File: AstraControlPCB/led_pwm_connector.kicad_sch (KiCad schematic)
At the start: 12 parts, among them CN5 JST_VH_8PIN_10A_250V

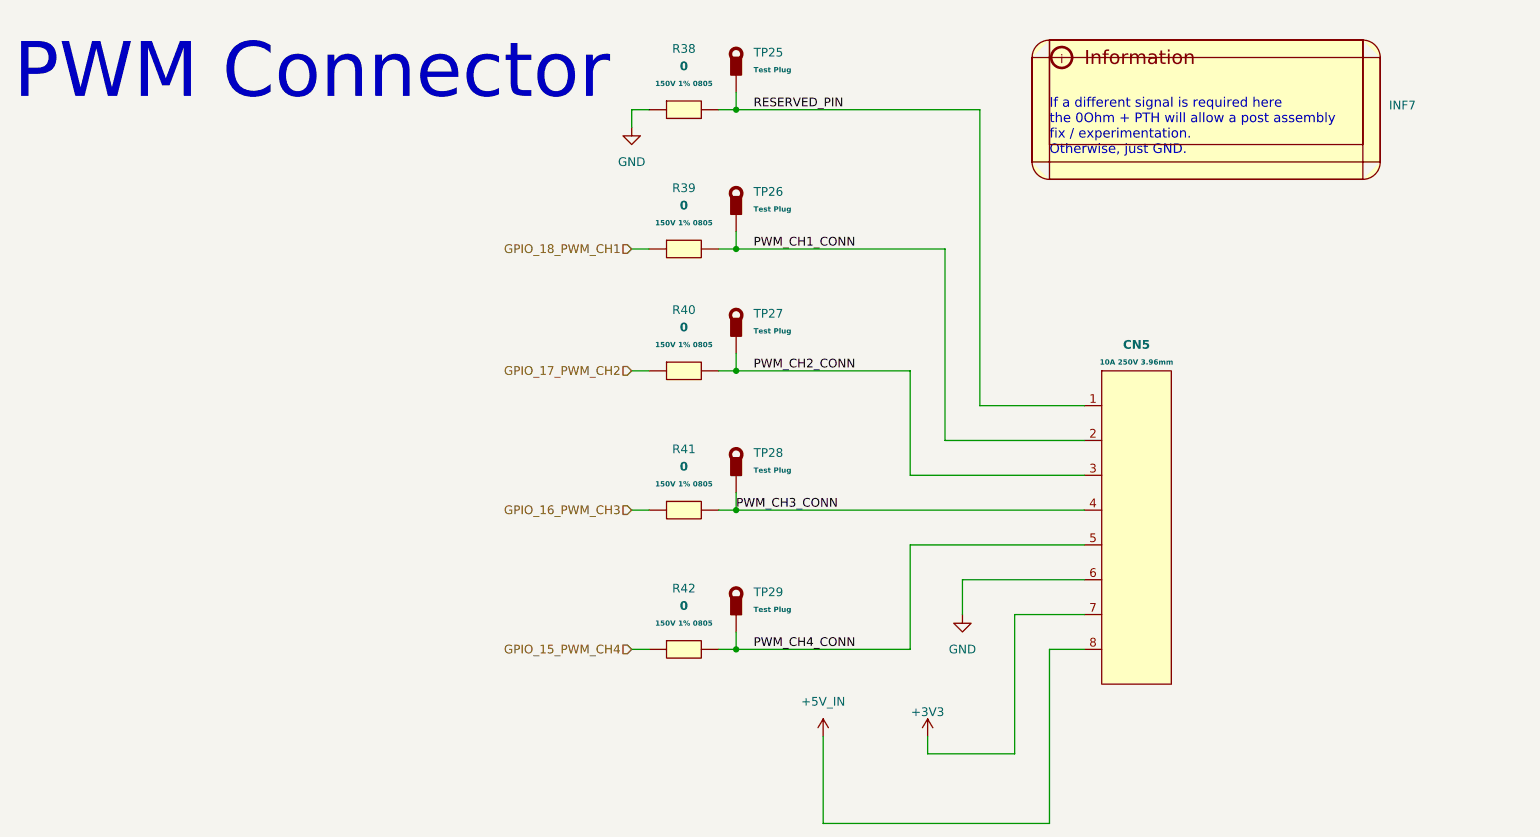
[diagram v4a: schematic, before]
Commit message: New inductor that is in stock, updated rs485 ic layout to put caps closer
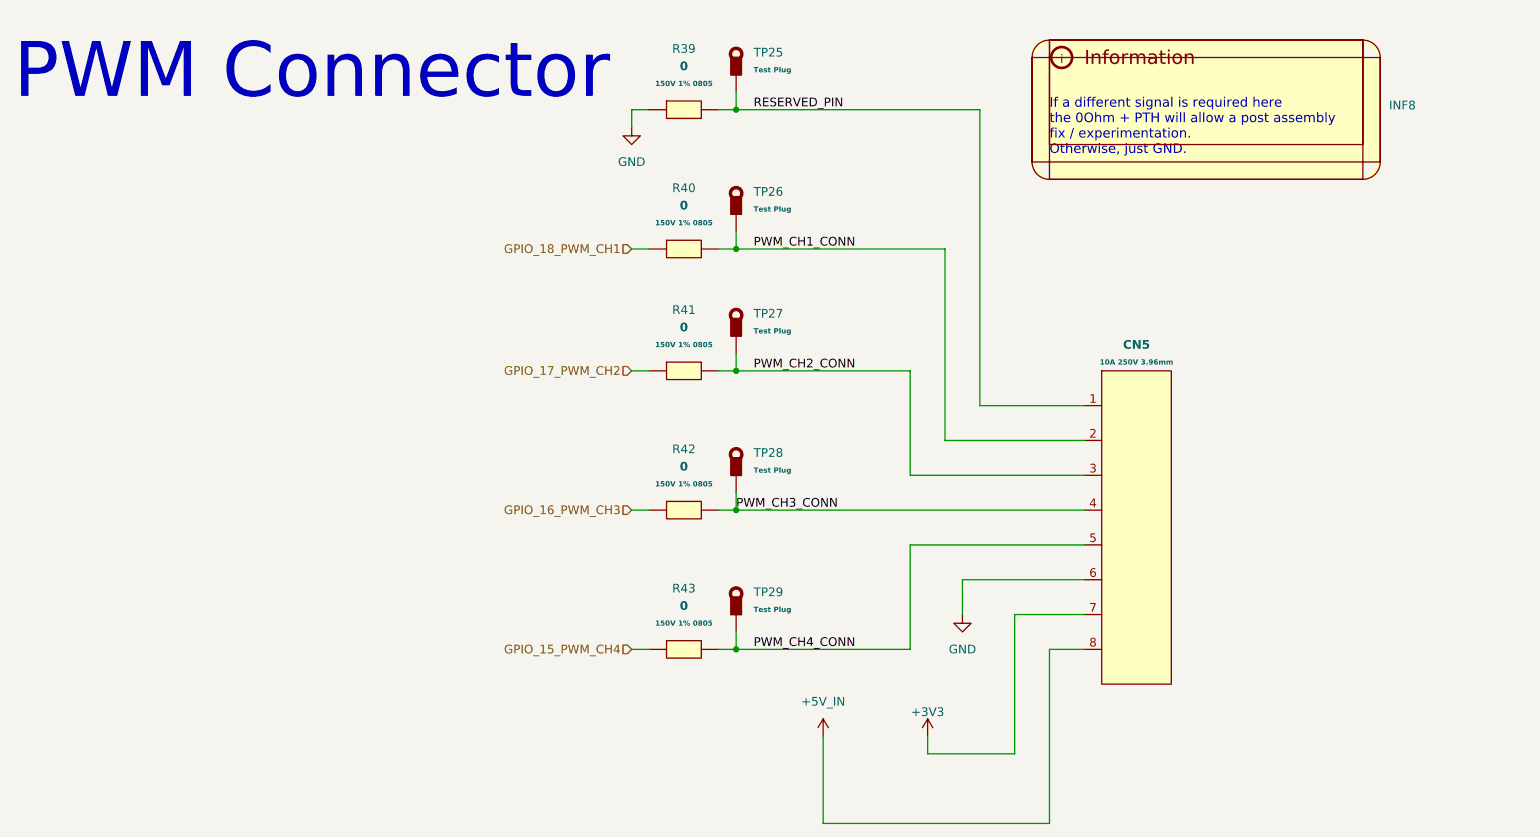
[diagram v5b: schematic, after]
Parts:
- renumbered INF7 to INF8, R38 to R39, R39 to R40, R40 to R41, R41 to R42, R42 to R43
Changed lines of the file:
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@@
 		(dnp no)
 		(fields_autoplaced yes)
-		(property "Reference" "#PWR072"
+		(property "Reference" "#PWR073"
 			(at 137.16 130.81 0)
 			(effects
@@
 			(project "AstraControl"
 				(path "/9a751838-dce8-4d69-8a02-736625ac74e7/0db21d8e-3390-4d67-877f-0e5d98e37848/e7f4ae23-1ac9-4fa3-959c-a78f85f3f546"
-					(reference "#PWR072")
+					(reference "#PWR073")
 					(unit 1)
 				)
@@
 		(on_board yes)
 		(dnp no)
-		(property "Reference" "#PWR073"
+		(property "Reference" "#PWR074"
 			(at 152.4 130.81 0)
 			(effects
@@
 			(project "AstraControl"
 				(path "/9a751838-dce8-4d69-8a02-736625ac74e7/0db21d8e-3390-4d67-877f-0e5d98e37848/e7f4ae23-1ac9-4fa3-959c-a78f85f3f546"
-					(reference "#PWR073")
+					(reference "#PWR074")
 					(unit 1)
 				)
@@
 		(dnp no)
 		(fields_autoplaced yes)
-		(property "Reference" "R38"
+		(property "Reference" "R39"
 			(at 116.84 26.67 0)
 			(effects
@@
 			(project "AstraControl"
 				(path "/9a751838-dce8-4d69-8a02-736625ac74e7/0db21d8e-3390-4d67-877f-0e5d98e37848/e7f4ae23-1ac9-4fa3-959c-a78f85f3f546"
-					(reference "R38")
+					(reference "R39")
 					(unit 1)
 				)
@@
 		(dnp no)
 		(fields_autoplaced yes)
-		(property "Reference" "#PWR074"
+		(property "Reference" "#PWR075"
 			(at 157.48 115.57 0)
 			(effects
@@
 			(project "AstraControl"
 				(path "/9a751838-dce8-4d69-8a02-736625ac74e7/0db21d8e-3390-4d67-877f-0e5d98e37848/e7f4ae23-1ac9-4fa3-959c-a78f85f3f546"
-					(reference "#PWR074")
+					(reference "#PWR075")
 					(unit 1)
 				)
@@
 		(dnp no)
 		(fields_autoplaced yes)
-		(property "Reference" "R40"
+		(property "Reference" "R41"
 			(at 116.84 64.77 0)
 			(effects
@@
 			(project "AstraControl"
 				(path "/9a751838-dce8-4d69-8a02-736625ac74e7/0db21d8e-3390-4d67-877f-0e5d98e37848/e7f4ae23-1ac9-4fa3-959c-a78f85f3f546"
-					(reference "R40")
+					(reference "R41")
 					(unit 1)
 				)
@@
 		(dnp no)
 		(fields_autoplaced yes)
-		(property "Reference" "R39"
+		(property "Reference" "R40"
 			(at 116.84 46.99 0)
 			(effects
@@
 			(project "AstraControl"
 				(path "/9a751838-dce8-4d69-8a02-736625ac74e7/0db21d8e-3390-4d67-877f-0e5d98e37848/e7f4ae23-1ac9-4fa3-959c-a78f85f3f546"
-					(reference "R39")
+					(reference "R40")
 					(unit 1)
 				)
@@
 		(dnp no)
 		(fields_autoplaced yes)
-		(property "Reference" "INF7"
+		(property "Reference" "INF8"
 			(at 219.71 34.9249 0)
 			(effects
@@
 			(project ""
 				(path "/9a751838-dce8-4d69-8a02-736625ac74e7/0db21d8e-3390-4d67-877f-0e5d98e37848/e7f4ae23-1ac9-4fa3-959c-a78f85f3f546"
-					(reference "INF7")
+					(reference "INF8")
 					(unit 1)
 				)
@@
 		(dnp no)
 		(fields_autoplaced yes)
-		(property "Reference" "#PWR071"
+		(property "Reference" "#PWR072"
 			(at 109.22 44.45 0)
 			(effects
@@
 			(project "AstraControl"
 				(path "/9a751838-dce8-4d69-8a02-736625ac74e7/0db21d8e-3390-4d67-877f-0e5d98e37848/e7f4ae23-1ac9-4fa3-959c-a78f85f3f546"
-					(reference "#PWR071")
+					(reference "#PWR072")
 					(unit 1)
 				)
@@
 		(dnp no)
 		(fields_autoplaced yes)
-		(property "Reference" "R42"
+		(property "Reference" "R43"
 			(at 116.84 105.41 0)
 			(effects
@@
 			(project "AstraControl"
 				(path "/9a751838-dce8-4d69-8a02-736625ac74e7/0db21d8e-3390-4d67-877f-0e5d98e37848/e7f4ae23-1ac9-4fa3-959c-a78f85f3f546"
-					(reference "R42")
+					(reference "R43")
 					(unit 1)
 				)
@@
 		(dnp no)
 		(fields_autoplaced yes)
-		(property "Reference" "R41"
+		(property "Reference" "R42"
 			(at 116.84 85.09 0)
 			(effects
@@
 			(project "AstraControl"
 				(path "/9a751838-dce8-4d69-8a02-736625ac74e7/0db21d8e-3390-4d67-877f-0e5d98e37848/e7f4ae23-1ac9-4fa3-959c-a78f85f3f546"
-					(reference "R41")
-					(unit 1)
-				)
+					(reference "R42")
+					(unit 1)
+				)

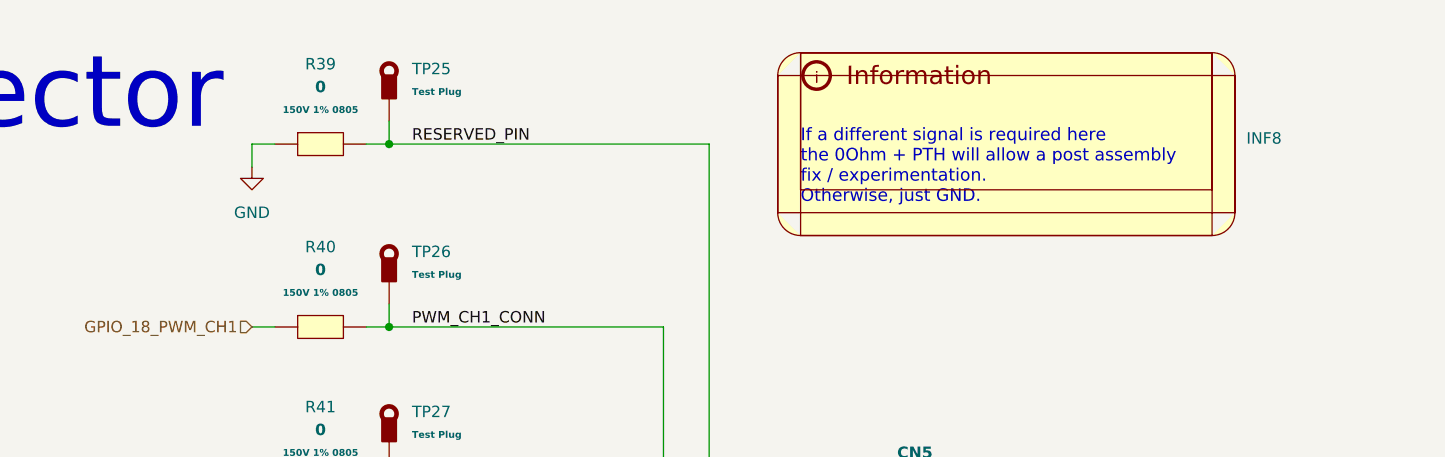
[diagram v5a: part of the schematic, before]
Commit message: Fix silkscreen on copper, add GPIO 8 to connector
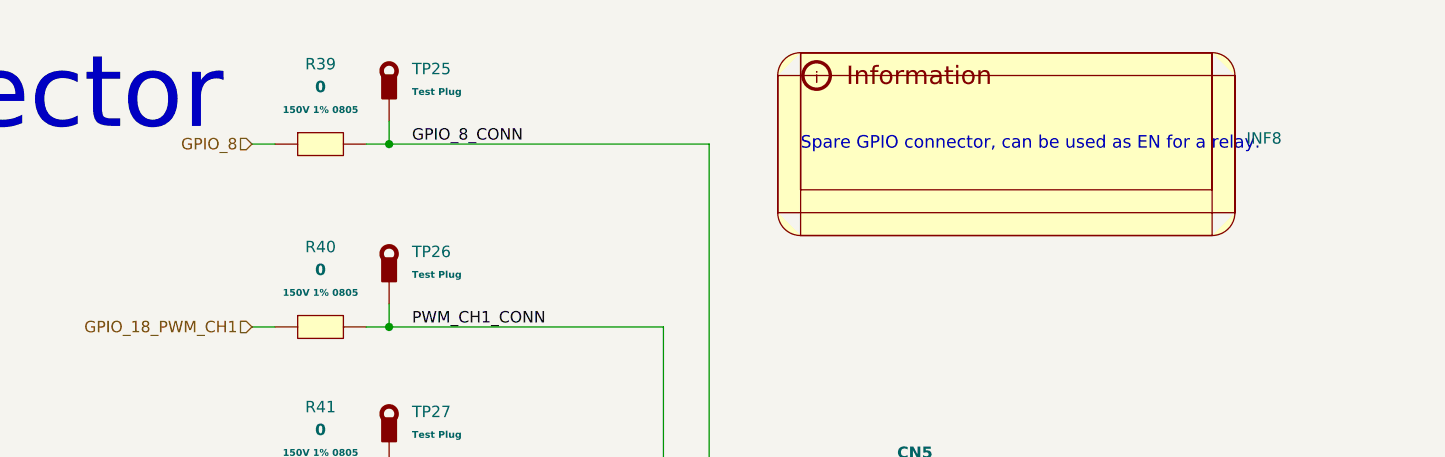
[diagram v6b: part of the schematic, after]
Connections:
- net GND: no longer R39.1
- net RESERVED_PIN renamed GPIO_8_CONN
- new net GPIO_8: R39.1
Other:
- note added: "Spare GPIO connector, can be used as EN for a relay."
- note removed: "If a different signal is required here the 0Ohm + PTH will allow a post assembly fix / experimentation. Otherwise, just GND."
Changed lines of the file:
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@@
-	(wire
-		(pts
-			(xy 109.22 35.56) (xy 109.22 38.1)
-		)
-		(stroke
-			(width 0)
-			(type default)
-		)
-	)
 	(wire
 		(pts
@@
 		)
 	)
-	(text "If a different signal is required here \nthe 0Ohm + PTH will allow a post assembly\nfix / experimentation.\nOtherwise, just GND."
+	(text "Spare GPIO connector, can be used as EN for a relay."
 		(exclude_from_sim no)
-		(at 170.18 38.1 0)
+		(at 170.18 35.56 0)
 		(effects
 			(font
@@
 		)
 	)
-	(label "RESERVED_PIN"
+	(label "GPIO_8_CONN"
 		(at 127 35.56 0)
 		(fields_autoplaced yes)
@@
 		(shape input)
 		(at 109.22 73.66 180)
+		(fields_autoplaced yes)
+		(effects
+			(font
+				(size 1.27 1.27)
+			)
+			(justify right)
+		)
+	)
+	(hierarchical_label "GPIO_8"
+		(shape input)
+		(at 109.22 35.56 180)
 		(fields_autoplaced yes)
 		(effects
@@
 		(dnp no)
 		(fields_autoplaced yes)
-		(property "Reference" "#PWR073"
+		(property "Reference" "#PWR072"
 			(at 137.16 130.81 0)
 			(effects
@@
 			(project "AstraControl"
 				(path "/9a751838-dce8-4d69-8a02-736625ac74e7/0db21d8e-3390-4d67-877f-0e5d98e37848/e7f4ae23-1ac9-4fa3-959c-a78f85f3f546"
-					(reference "#PWR073")
+					(reference "#PWR072")
 					(unit 1)
 				)
@@
 		(on_board yes)
 		(dnp no)
-		(property "Reference" "#PWR074"
+		(property "Reference" "#PWR073"
 			(at 152.4 130.81 0)
 			(effects
@@
 			(project "AstraControl"
 				(path "/9a751838-dce8-4d69-8a02-736625ac74e7/0db21d8e-3390-4d67-877f-0e5d98e37848/e7f4ae23-1ac9-4fa3-959c-a78f85f3f546"
-					(reference "#PWR074")
+					(reference "#PWR073")
 					(unit 1)
 				)
@@
 		(dnp no)
 		(fields_autoplaced yes)
-		(property "Reference" "#PWR075"
+		(property "Reference" "#PWR074"
 			(at 157.48 115.57 0)
 			(effects
@@
 			(project "AstraControl"
 				(path "/9a751838-dce8-4d69-8a02-736625ac74e7/0db21d8e-3390-4d67-877f-0e5d98e37848/e7f4ae23-1ac9-4fa3-959c-a78f85f3f546"
-					(reference "#PWR075")
+					(reference "#PWR074")
 					(unit 1)
 				)
@@
 					(unit 1)
 				)
-			)
-		)
-	)
-	(symbol
-		(lib_id "power:GND")
-		(at 109.22 38.1 0)
-		(unit 1)
-		(exclude_from_sim no)
-		(in_bom yes)
-		(on_board yes)
-		(dnp no)
-		(fields_autoplaced yes)
-		(property "Reference" "#PWR072"
-			(at 109.22 44.45 0)
-			(effects
-				(font
-					(size 1.27 1.27)
-				)
-				(hide yes)
-			)
-		)
-		(property "Value" "GND"
-			(at 109.22 43.18 0)
-			(effects
-				(font
-					(size 1.27 1.27)
-				)
-			)
-		)
-		(property "Footprint" ""
-			(at 109.22 38.1 0)
-			(effects
-				(font
-					(size 1.27 1.27)
-				)
-				(hide yes)
-			)
-		)
-		(property "Datasheet" ""
-			(at 109.22 38.1 0)
-			(effects
-				(font
-					(size 1.27 1.27)
-				)
-				(hide yes)
-			)
-		)
-		(property "Description" "Power symbol creates a global label with name \"GND\" , ground"
-			(at 109.22 38.1 0)
-			(effects
-				(font
-					(size 1.27 1.27)
-				)
-				(hide yes)
-			)
-		)
-		(pin "1"
-		)
-		(instances
-			(project "AstraControl"
-				(path "/9a751838-dce8-4d69-8a02-736625ac74e7/0db21d8e-3390-4d67-877f-0e5d98e37848/e7f4ae23-1ac9-4fa3-959c-a78f85f3f546"
-					(reference "#PWR072")
-					(unit 1)
-				)

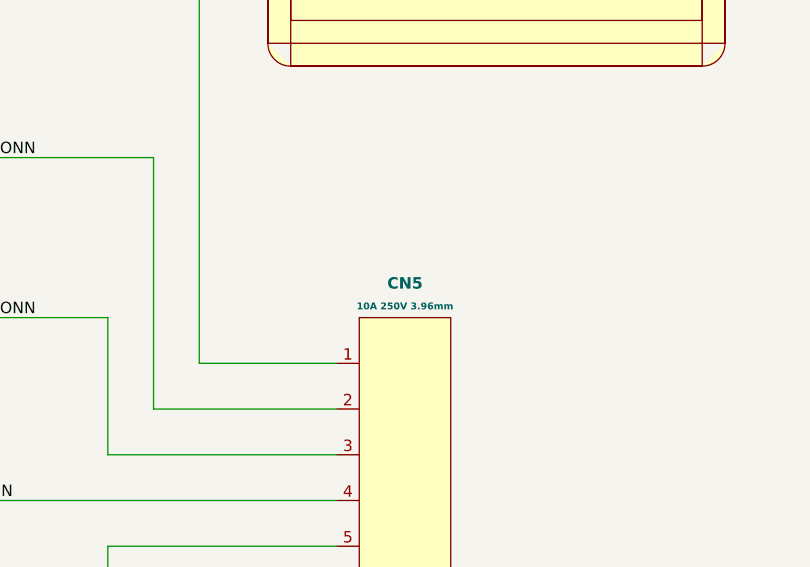
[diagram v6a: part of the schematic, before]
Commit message: Updated to JST SH, 3A diode for USB, added extra 2P VH
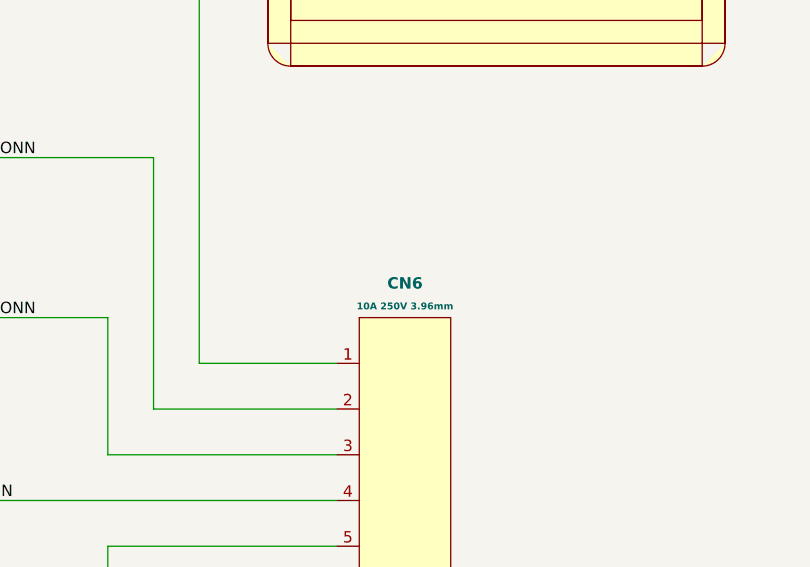
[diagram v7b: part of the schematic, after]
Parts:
- renumbered CN5 to CN6
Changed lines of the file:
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@@
 		(on_board yes)
 		(dnp no)
-		(property "Reference" "CN5"
+		(property "Reference" "CN6"
 			(at 182.88 69.85 0)
 			(effects
@@
 			(project "AstraControl"
 				(path "/9a751838-dce8-4d69-8a02-736625ac74e7/0db21d8e-3390-4d67-877f-0e5d98e37848/e7f4ae23-1ac9-4fa3-959c-a78f85f3f546"
-					(reference "CN5")
+					(reference "CN6")
 					(unit 1)
 				)
@@
 		(dnp no)
 		(fields_autoplaced yes)
-		(property "Reference" "#PWR072"
+		(property "Reference" "#PWR076"
 			(at 137.16 130.81 0)
 			(effects
@@
 			(project "AstraControl"
 				(path "/9a751838-dce8-4d69-8a02-736625ac74e7/0db21d8e-3390-4d67-877f-0e5d98e37848/e7f4ae23-1ac9-4fa3-959c-a78f85f3f546"
-					(reference "#PWR072")
+					(reference "#PWR076")
 					(unit 1)
 				)
@@
 		(on_board yes)
 		(dnp no)
-		(property "Reference" "#PWR073"
+		(property "Reference" "#PWR077"
 			(at 152.4 130.81 0)
 			(effects
@@
 			(project "AstraControl"
 				(path "/9a751838-dce8-4d69-8a02-736625ac74e7/0db21d8e-3390-4d67-877f-0e5d98e37848/e7f4ae23-1ac9-4fa3-959c-a78f85f3f546"
-					(reference "#PWR073")
+					(reference "#PWR077")
 					(unit 1)
 				)
@@
 		(dnp no)
 		(fields_autoplaced yes)
-		(property "Reference" "#PWR074"
+		(property "Reference" "#PWR078"
 			(at 157.48 115.57 0)
 			(effects
@@
 			(project "AstraControl"
 				(path "/9a751838-dce8-4d69-8a02-736625ac74e7/0db21d8e-3390-4d67-877f-0e5d98e37848/e7f4ae23-1ac9-4fa3-959c-a78f85f3f546"
-					(reference "#PWR074")
+					(reference "#PWR078")
 					(unit 1)
 				)

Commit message: Update revision and add year to silkscreen
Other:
- title: AstraControl - PWM Connector -> AstraControl - Root
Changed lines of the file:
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@@
 	(paper "A4")
 	(title_block
-		(title "AstraControl - PWM Connector")
+		(title "AstraControl - Root")
 		(date "2024-08-26")
-		(rev "A")
+		(rev "B")
 		(company "LiveAstra Technologies")
 	)
